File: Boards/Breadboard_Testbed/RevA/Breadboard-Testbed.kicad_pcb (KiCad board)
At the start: 2 copper layers, 85 x 56 mm, 13 parts, among them J1 main_conn_10, J10 Arduino-right, J11 Arduino-right, J12 Conn_02x12_Counter_Clockwise, J2 main_conn_12, J3 Conn_02x10_Counter_Clockwise, J4 Conn_02x10_Counter_Clockwise, J5 Conn_02x10_Counter_Clockwise, J6 Arduino-left, J7 Arduino-left, J8 Conn_02x10_Counter_Clockwise, J9 Conn_02x12_Counter_Clockwise

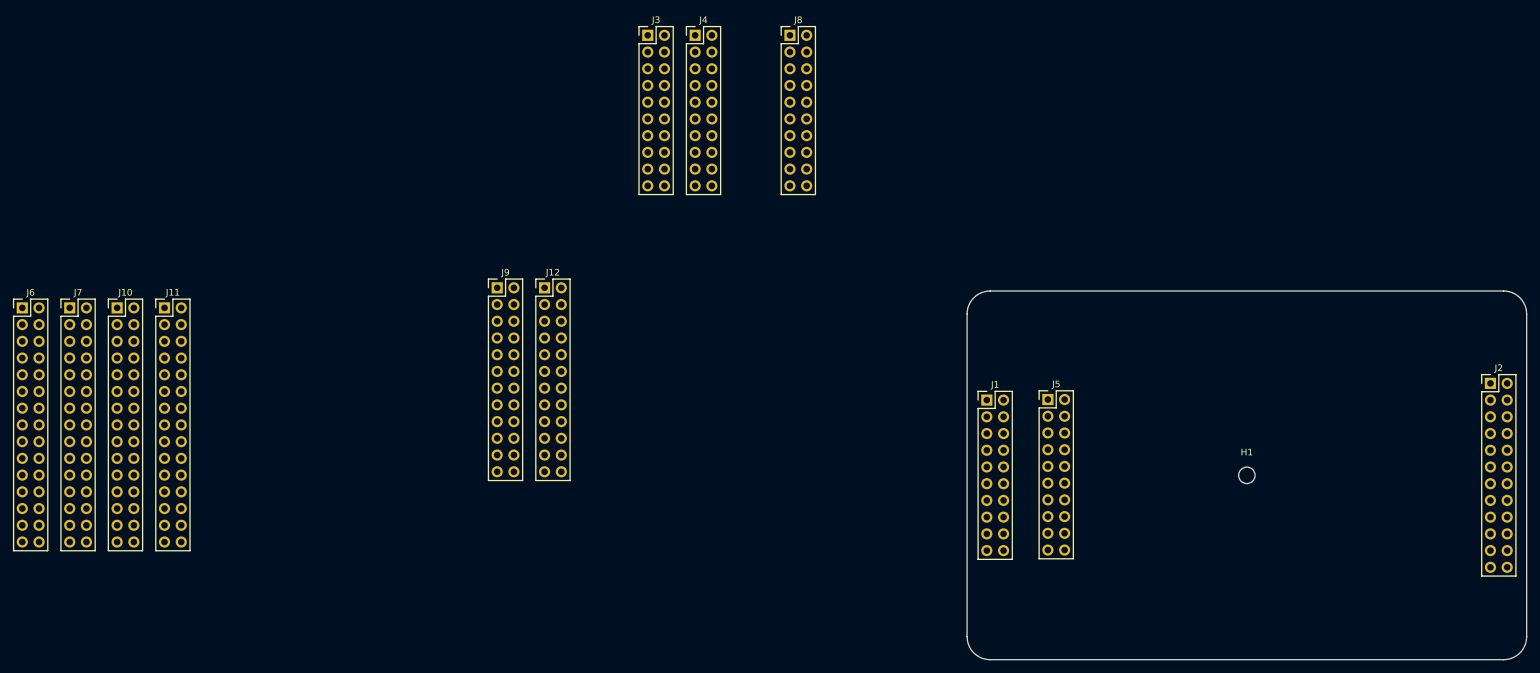
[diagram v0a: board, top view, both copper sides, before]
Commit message: Finished Test-RevA layout Pre-route
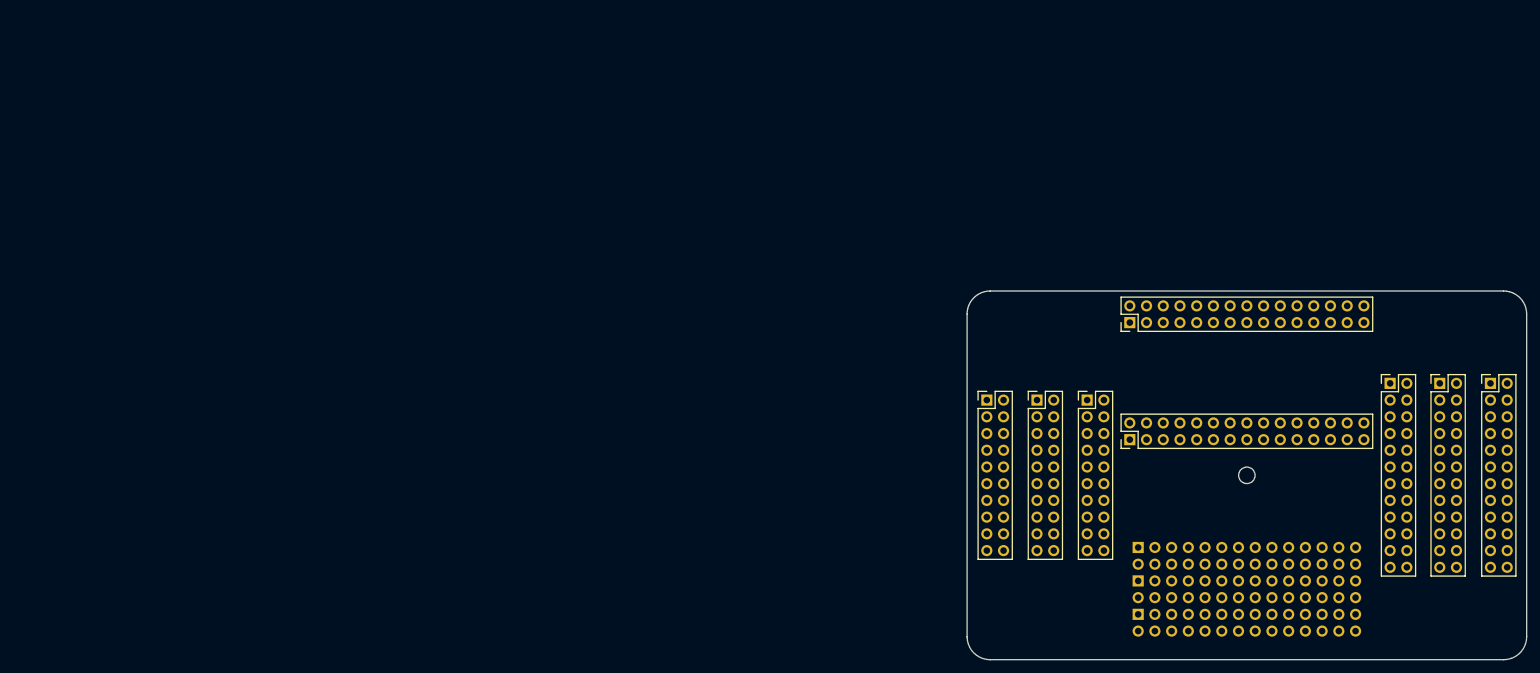
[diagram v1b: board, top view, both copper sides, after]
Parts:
- removed J11: Arduino-right, Connector_PinHeader_2.54mm:PinHeader_2x15_P2.54mm_Vertical
- J3, J4: value Conn_02x10_Counter_Clockwise -> Conn_02x14_Odd_Even; footprint Connector_PinHeader_2.54mm:PinHeader_2x10_P2.54mm_Vertical -> Connector_PinHeader_2.54mm:PinHeader_2x14_P2.54mm_Vertical; moved to B.Cu
- J6: value Arduino-left -> Conn_02x14_Odd_Even; footprint Connector_PinHeader_2.54mm:PinHeader_2x15_P2.54mm_Vertical -> Connector_PinHeader_2.54mm:PinHeader_2x14_P2.54mm_Vertical; moved to B.Cu
- moved J6 175.8 mm to (186.0, 119.1), turned to 270 degrees
- moved J7 162.3 mm to (184.7, 92.6), turned to 90 degrees
- moved J10 153.8 mm to (184.7, 74.8), turned to 90 degrees
- moved J12 136.7 mm to (231.8, 84.0)
- moved J9 136.4 mm to (224.3, 84.0)
- moved J3 107.7 mm to (186.0, 109.0), turned to 270 degrees
- moved J4 106.8 mm to (186.0, 114.0), turned to 270 degrees
- moved J8 71.5 mm to (178.2, 86.6)
- moved J5 1.66 mm to (170.6, 86.6)
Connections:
- net /3v3 renamed Net-(J1-Pad1)
- net /3v3_2 renamed Net-(J1-Pad8)
- net /5v renamed Net-(J1-Pad3)
- net /5v2 renamed Net-(J1-Pad7)
- net /gnd renamed Net-(J1-Pad11)
- net /gnd2 renamed Net-(J1-Pad17)
- net /gnd3 renamed Net-(J1-Pad14)
- net /gnd4 renamed Net-(J1-Pad2)
- net /gpio1 renamed Net-(J1-Pad13)
- net /gpio11 renamed Net-(J1-Pad16)
- net /gpio6 renamed Net-(J1-Pad12)
- net /gpio7 renamed Net-(J1-Pad10)
- net /gpio8 renamed Net-(J1-Pad6)
- net /mosi renamed Net-(J1-Pad4)
- net /scl2 renamed Net-(J1-Pad9)
- net /sda2 renamed Net-(J1-Pad5)
- net /spi2_ce0 renamed Net-(J1-Pad18)
- net /spi2_ce1 renamed Net-(J1-Pad20)
- net /uart_rx renamed Net-(J1-Pad19)
- net /uart_tx renamed Net-(J1-Pad15)
- J10 pad 12: Net-(J10-Pad12) -> Net-(J10-Pad11)
- J10 pad 14: Net-(J10-Pad14) -> Net-(J10-Pad13)
- J10 pad 16: Net-(J10-Pad16) -> Net-(J10-Pad15)
- J10 pad 18: Net-(J10-Pad18) -> Net-(J10-Pad17)
- J10 pad 2: Net-(J10-Pad2) -> Net-(J10-Pad1)
- J10 pad 20: Net-(J10-Pad20) -> Net-(J10-Pad19)
- J10 pad 22: Net-(J10-Pad22) -> Net-(J10-Pad21)
- J10 pad 24: Net-(J10-Pad24) -> Net-(J10-Pad23)
- J10 pad 26: Net-(J10-Pad26) -> Net-(J10-Pad25)
- J10 pad 28: Net-(J10-Pad28) -> Net-(J10-Pad27)
- J10 pad 30: Net-(J10-Pad30) -> Net-(J10-Pad29)
- J10 pad 4: Net-(J10-Pad4) -> Net-(J10-Pad3)
- J10 pad 6: Net-(J10-Pad6) -> Net-(J10-Pad5)
- J10 pad 8: Net-(J10-Pad8) -> Net-(J10-Pad7)
- J10 pad 9: Net-(J10-Pad9) -> Net-(J10-Pad10)
- J12 pad 1: /miso -> Net-(J12-Pad1)
- J12 pad 10: /gnd_3 -> Net-(J12-Pad10)
- J12 pad 11: /spi_ce1 -> Net-(J12-Pad11)
- J12 pad 12: /spi_ce1 -> Net-(J12-Pad11)
- J12 pad 13: /sda -> Net-(J12-Pad13)
- J12 pad 14: /sda -> Net-(J12-Pad13)
- J12 pad 15: /scl -> Net-(J12-Pad15)
- J12 pad 16: /scl -> Net-(J12-Pad15)
- J12 pad 17: /gpio2 -> Net-(J12-Pad17)
- J12 pad 18: /gpio2 -> Net-(J12-Pad17)
- J12 pad 19: /gnd_2 -> Net-(J12-Pad19)
- J12 pad 2: /miso -> Net-(J12-Pad1)
- J12 pad 20: /gnd_2 -> Net-(J12-Pad19)
- J12 pad 21: /gpio3 -> Net-(J12-Pad21)
- J12 pad 22: /gpio3 -> Net-(J12-Pad21)
- J12 pad 23: /gpio4 -> Net-(J12-Pad23)
- J12 pad 24: /gpio4 -> Net-(J12-Pad23)
- J12 pad 3: /gpio9 -> Net-(J12-Pad3)
- J12 pad 4: /gpio9 -> Net-(J12-Pad3)
- J12 pad 5: /sclk -> Net-(J12-Pad5)
- J12 pad 6: /sclk -> Net-(J12-Pad5)
- J12 pad 7: /spi_ce0 -> Net-(J12-Pad7)
- J12 pad 8: /spi_ce0 -> Net-(J12-Pad7)
- J12 pad 9: /gnd_3 -> Net-(J12-Pad10)
- J2 pad 1: /miso -> Net-(J2-Pad1)
- J2 pad 10: /sclk2 -> Net-(J12-Pad10)
- J2 pad 11: /spi_ce1 -> Net-(J2-Pad11)
- J2 pad 12: /gnd_ -> Net-(J12-Pad11)
- J2 pad 13: /sda -> Net-(J2-Pad13)
- J2 pad 14: /miso2 -> Net-(J12-Pad13)
- J2 pad 15: /scl -> Net-(J2-Pad15)
- J2 pad 16: /gpio10 -> Net-(J12-Pad15)
- J2 pad 17: /gpio2 -> Net-(J2-Pad17)
- J2 pad 18: /spi2_ce2 -> Net-(J12-Pad17)
- J2 pad 19: /gnd_2 -> Net-(J2-Pad19)
- J2 pad 2: /vcc1 -> Net-(J12-Pad1)
- J2 pad 20: /miso2_pwm -> Net-(J12-Pad19)
- J2 pad 21: /gpio3 -> Net-(J2-Pad21)
- J2 pad 22: /gnd_1 -> Net-(J12-Pad21)
- J2 pad 23: /gpio4 -> Net-(J2-Pad23)
- J2 pad 24: /gpio5 -> Net-(J12-Pad23)
- J2 pad 3: /gpio9 -> Net-(J2-Pad3)
- J2 pad 4: /vcc -> Net-(J12-Pad3)
- J2 pad 5: /sclk -> Net-(J2-Pad5)
- J2 pad 6: /reset -> Net-(J12-Pad5)
- J2 pad 7: /spi_ce0 -> Net-(J2-Pad7)
- J2 pad 8: /NC -> Net-(J12-Pad7)
- J2 pad 9: /gnd_3 -> Net-(J2-Pad9)
- J6 pad 1: Net-(J6-Pad1) -> Net-(J3-Pad1)
- J6 pad 10: Net-(J6-Pad10) -> Net-(J3-Pad10)
- J6 pad 11: Net-(J6-Pad11) -> Net-(J3-Pad11)
- J6 pad 12: Net-(J6-Pad12) -> Net-(J3-Pad11)
- J6 pad 13: Net-(J6-Pad13) -> Net-(J3-Pad13)
- J6 pad 14: Net-(J6-Pad14) -> Net-(J3-Pad13)
- J6 pad 15: Net-(J6-Pad15) -> Net-(J3-Pad15)
- J6 pad 16: Net-(J6-Pad16) -> Net-(J3-Pad15)
- J6 pad 17: Net-(J6-Pad17) -> Net-(J3-Pad17)
- J6 pad 18: Net-(J6-Pad18) -> Net-(J3-Pad17)
- J6 pad 19: Net-(J6-Pad19) -> Net-(J3-Pad19)
- J6 pad 2: Net-(J6-Pad2) -> Net-(J3-Pad1)
- J6 pad 20: Net-(J6-Pad20) -> Net-(J3-Pad19)
- J6 pad 21: Net-(J6-Pad21) -> Net-(J3-Pad21)
- J6 pad 22: Net-(J6-Pad22) -> Net-(J3-Pad21)
- J6 pad 23: Net-(J6-Pad23) -> Net-(J3-Pad23)
- J6 pad 24: Net-(J6-Pad24) -> Net-(J3-Pad23)
- J6 pad 25: Net-(J6-Pad25) -> Net-(J3-Pad25)
- J6 pad 26: Net-(J6-Pad26) -> Net-(J3-Pad25)
- J6 pad 27: Net-(J6-Pad27) -> Net-(J3-Pad27)
- J6 pad 28: Net-(J6-Pad28) -> Net-(J3-Pad27)
- J6 pad 3: Net-(J6-Pad3) -> Net-(J3-Pad3)
- J6 pad 4: Net-(J6-Pad4) -> Net-(J3-Pad3)
- J6 pad 5: Net-(J6-Pad5) -> Net-(J3-Pad5)
- J6 pad 6: Net-(J6-Pad6) -> Net-(J3-Pad5)
- J6 pad 7: Net-(J6-Pad7) -> Net-(J3-Pad7)
- J6 pad 8: Net-(J6-Pad8) -> Net-(J3-Pad7)
- J6 pad 9: Net-(J6-Pad9) -> Net-(J3-Pad10)
- J7 pad 1: Net-(J6-Pad2) -> Net-(J7-Pad1)
- J7 pad 10: Net-(J6-Pad9) -> Net-(J7-Pad10)
- J7 pad 11: Net-(J6-Pad12) -> Net-(J7-Pad11)
- J7 pad 12: Net-(J6-Pad11) -> Net-(J7-Pad11)
- J7 pad 13: Net-(J6-Pad14) -> Net-(J7-Pad13)
- J7 pad 14: Net-(J6-Pad13) -> Net-(J7-Pad13)
- J7 pad 15: Net-(J6-Pad16) -> Net-(J7-Pad15)
- J7 pad 16: Net-(J6-Pad15) -> Net-(J7-Pad15)
- J7 pad 17: Net-(J6-Pad18) -> Net-(J7-Pad17)
- J7 pad 18: Net-(J6-Pad17) -> Net-(J7-Pad17)
- J7 pad 19: Net-(J6-Pad20) -> Net-(J7-Pad19)
- J7 pad 2: Net-(J6-Pad1) -> Net-(J7-Pad1)
- J7 pad 20: Net-(J6-Pad19) -> Net-(J7-Pad19)
- J7 pad 21: Net-(J6-Pad22) -> Net-(J7-Pad21)
- J7 pad 22: Net-(J6-Pad21) -> Net-(J7-Pad21)
- J7 pad 23: Net-(J6-Pad24) -> Net-(J7-Pad23)
- J7 pad 24: Net-(J6-Pad23) -> Net-(J7-Pad23)
- J7 pad 25: Net-(J6-Pad26) -> Net-(J7-Pad25)
- J7 pad 26: Net-(J6-Pad25) -> Net-(J7-Pad25)
- J7 pad 27: Net-(J6-Pad28) -> Net-(J7-Pad27)
- J7 pad 28: Net-(J6-Pad27) -> Net-(J7-Pad27)
- J7 pad 29: Net-(J6-Pad30) -> Net-(J7-Pad29)
- J7 pad 3: Net-(J6-Pad4) -> Net-(J7-Pad3)
- J7 pad 30: Net-(J6-Pad29) -> Net-(J7-Pad29)
- J7 pad 4: Net-(J6-Pad3) -> Net-(J7-Pad3)
- J7 pad 5: Net-(J6-Pad6) -> Net-(J7-Pad5)
- J7 pad 6: Net-(J6-Pad5) -> Net-(J7-Pad5)
- J7 pad 7: Net-(J6-Pad8) -> Net-(J7-Pad7)
- J7 pad 8: Net-(J6-Pad7) -> Net-(J7-Pad7)
- J7 pad 9: Net-(J6-Pad10) -> Net-(J7-Pad10)
- J9 pad 1: /vcc1 -> Net-(J2-Pad1)
- J9 pad 10: /sclk2 -> Net-(J2-Pad9)
- J9 pad 11: /gnd_ -> Net-(J2-Pad11)
- J9 pad 12: /gnd_ -> Net-(J2-Pad11)
- J9 pad 13: /miso2 -> Net-(J2-Pad13)
- J9 pad 14: /miso2 -> Net-(J2-Pad13)
- J9 pad 15: /gpio10 -> Net-(J2-Pad15)
- J9 pad 16: /gpio10 -> Net-(J2-Pad15)
- J9 pad 17: /spi2_ce2 -> Net-(J2-Pad17)
- J9 pad 18: /spi2_ce2 -> Net-(J2-Pad17)
- J9 pad 19: /miso2_pwm -> Net-(J2-Pad19)
- J9 pad 2: /vcc1 -> Net-(J2-Pad1)
- J9 pad 20: /miso2_pwm -> Net-(J2-Pad19)
- J9 pad 21: /gnd_1 -> Net-(J2-Pad21)
- J9 pad 22: /gnd_1 -> Net-(J2-Pad21)
- J9 pad 23: /gpio5 -> Net-(J2-Pad23)
- J9 pad 24: /gpio5 -> Net-(J2-Pad23)
- J9 pad 3: /vcc -> Net-(J2-Pad3)
- J9 pad 4: /vcc -> Net-(J2-Pad3)
- J9 pad 5: /reset -> Net-(J2-Pad5)
- J9 pad 6: /reset -> Net-(J2-Pad5)
- J9 pad 7: /NC -> Net-(J2-Pad7)
- J9 pad 8: /NC -> Net-(J2-Pad7)
- J9 pad 9: /sclk2 -> Net-(J2-Pad9)

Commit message: Routing Complete  Test-RevA board
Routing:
- net Net-(J2-Pad9): track 0.00 -> 16.2 mm
- net Net-(J2-Pad5): track 0.00 -> 16.2 mm
- net Net-(J2-Pad3): track 0.00 -> 16.2 mm
- net Net-(J2-Pad17): track 0.00 -> 16.2 mm
- net Net-(J2-Pad15): track 0.00 -> 16.2 mm
- net Net-(J2-Pad11): track 0.00 -> 16.2 mm
- net Net-(J1-Pad20): track 0.00 -> 16.2 mm
- net Net-(J1-Pad18): track 0.00 -> 16.2 mm
- net Net-(J1-Pad14): track 0.00 -> 16.2 mm
- net Net-(J1-Pad12): track 0.00 -> 16.2 mm
- net Net-(J2-Pad7): track 0.00 -> 16.2 mm
- net Net-(J1-Pad16): track 0.00 -> 16.2 mm
- net Net-(J2-Pad23): track 0.00 -> 16.2 mm
- net Net-(J2-Pad21): track 0.00 -> 16.2 mm
- net Net-(J2-Pad19): track 0.00 -> 16.2 mm
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
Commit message: Testbed-RevA postroute complete
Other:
- board text added: "A"
- board text added: "Arduino"
- board text added: "B"
- board text added: "Breadboard"
- board text added: "C"
- board text added: "D"
- board text added: "JLCJLCJLCJLC"
- board text added: "SDAQ Testing Platform Revision A"
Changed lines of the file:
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@@
   (general
     (thickness 1.6)
-    (drawings 9)
+    (drawings 21)
     (tracks 386)
     (zones 0)
@@
     )
   )
+  (gr_text "SDAQ Testing Platform Revision A" (at 202.692 86.1695) (layer B.SilkS)
+    (effects (font (size 1.5 1.5) (thickness 0.2)) (justify mirror))
+  )
+  (gr_text D (at 233.299 80.899) (layer F.SilkS)
+    (effects (font (size 2 2) (thickness 0.25)))
+  )
+  (gr_text D (at 241.9985 80.899) (layer F.SilkS)
+    (effects (font (size 2 2) (thickness 0.25)))
+  )
+  (gr_text C (at 225.4885 80.8355) (layer F.SilkS)
+    (effects (font (size 2 2) (thickness 0.25)))
+  )
+  (gr_text C (at 239.4585 80.899) (layer F.SilkS)
+    (effects (font (size 2 2) (thickness 0.25)))
+  )
+  (gr_text B (at 179.6415 82.931) (layer F.SilkS)
+    (effects (font (size 2 2) (thickness 0.25)))
+  )
+  (gr_text B (at 165.608 82.9945) (layer F.SilkS)
+    (effects (font (size 2 2) (thickness 0.25)))
+  )
+  (gr_text A (at 171.958 82.8675) (layer F.SilkS)
+    (effects (font (size 2 2) (thickness 0.25)))
+  )
+  (gr_text A (at 162.941 82.931) (layer F.SilkS)
+    (effects (font (size 2 2) (thickness 0.25)))
+  )
+  (gr_text JLCJLCJLCJLC (at 171.958 74.549) (layer B.SilkS)
+    (effects (font (size 2 2) (thickness 0.25)) (justify mirror))
+  )
+  (gr_text Breadboard (at 202.565 105.537) (layer F.SilkS)
+    (effects (font (size 2 2) (thickness 0.25)))
+  )
+  (gr_text Arduino (at 201.3585 82.3595) (layer F.SilkS)
+    (effects (font (size 3 3) (thickness 0.75)))
+  )
   (gr_line (start 155.829 98) (end 252.476 98) (layer Dwgs.User) (width 0.15))
